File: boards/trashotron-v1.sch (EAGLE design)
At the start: 6 parts, among them IC1 MCP604P, IC2 MCP604P, J3 455-1750-1-ND

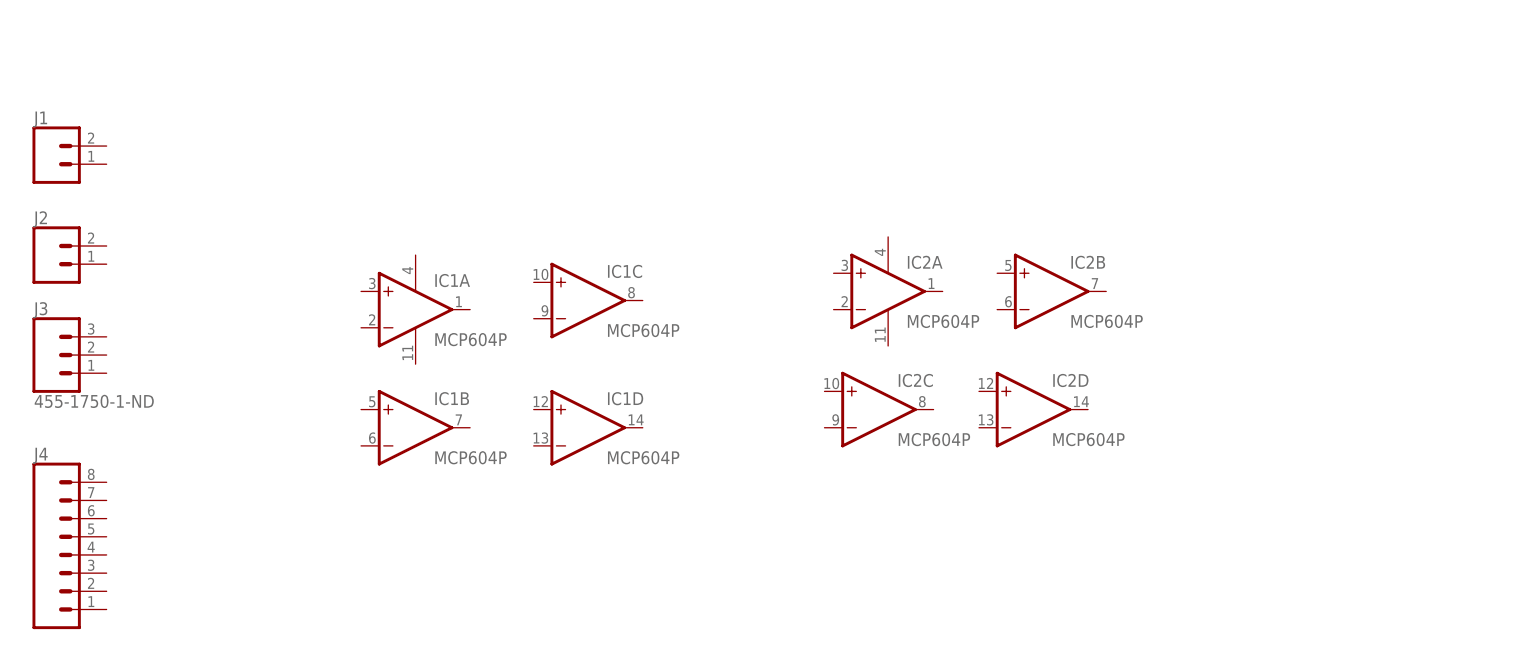
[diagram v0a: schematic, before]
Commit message: trashotron board mostly laid out in schematic
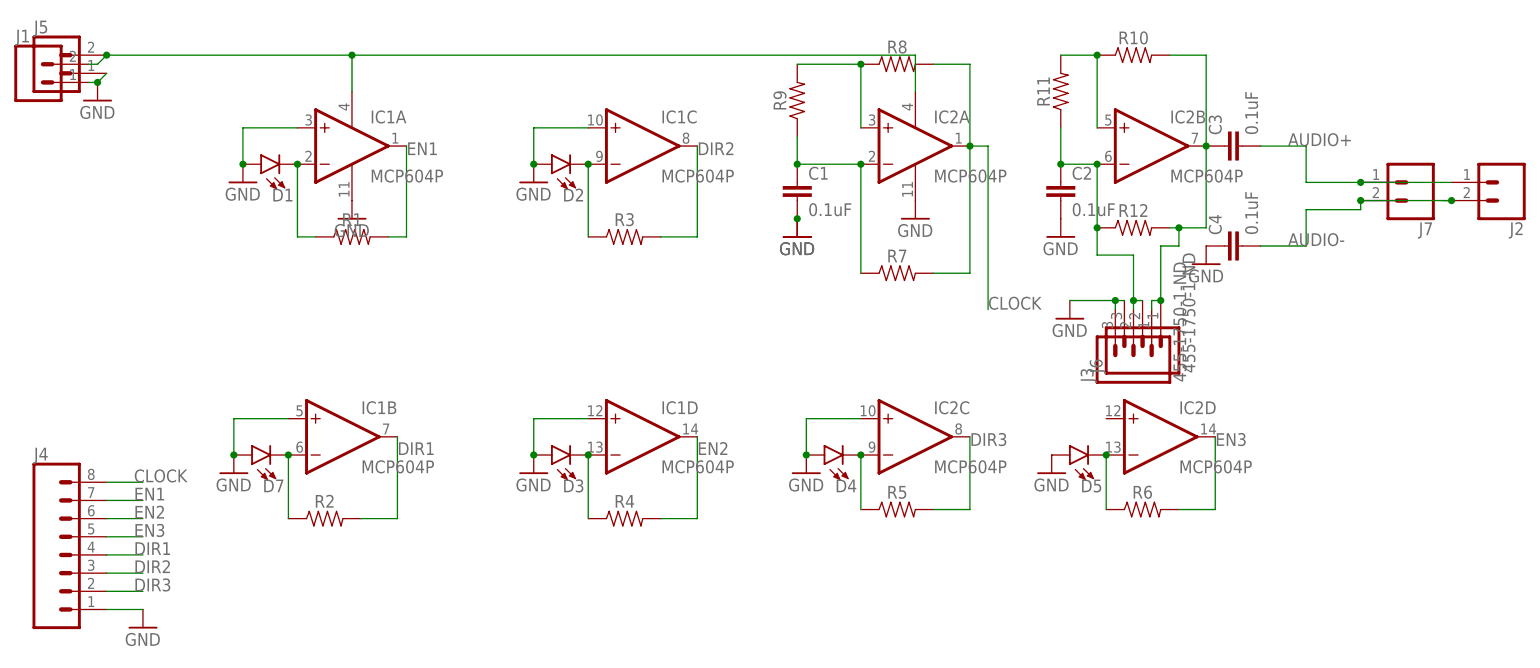
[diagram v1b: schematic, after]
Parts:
- added C1, C2, C3, C4: 0.1uF, SparkFun-Capacitors:0.1UF-KIT-EZ-50V-20%
- added D1, D2, D3, D4, D5, D7: (no value), SparkFun-LED:LED3MM
- added J5, J7: (no value), SparkFun-Connectors:CONN_02
- added J6: 455-1750-1-ND, SparkFun-Connectors:CONN_03
- added R1, R10, R11, R12, R2, R3, R4, R5, R6, R7, R8, R9: (no value), SparkFun-Resistors:RESISTORAXIAL-0.3
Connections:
- new net AUDIO+: C3.2, J2.1, J7.1
- new net AUDIO-: C4.2, J2.2, J7.2
- new net CLOCK: IC2A.OUT, J4.8, R7.2, R8.2
- new net DIR1: IC1B.OUT, J4.4, R2.2
- new net DIR2: IC1C.OUT, J4.3, R3.2
- new net DIR3: IC2C.OUT, J4.2, R5.2
- new net EN1: IC1A.OUT, J4.7, R1.2
- new net EN2: IC1D.OUT, J4.6, R4.2
- new net EN3: IC2D.OUT, J4.5, R6.2
- new net GND: C1.2, C2.2, C4.1, D1.A, D2.A, D3.A, D4.A, D5.A, D7.A, IC1A.+IN, IC1B.+IN, IC1C.+IN, IC1D.+IN, IC1P.V-, IC2C.+IN, IC2P.V-, J1.1, J3.3, J4.1, J5.1, J6.3
- new net N$1: D1.C, IC1A.-IN, R1.1
- new net N$11: D5.C, IC2D.-IN, R6.1
- new net N$13: D3.C, IC1D.-IN, R4.1
- new net N$15: C2.1, IC2B.-IN, J3.2, J6.2, R11.1, R12.1
- new net N$16: IC2A.+IN, R8.1, R9.2
- new net N$18: IC2B.+IN, R10.1, R11.2
- new net N$19: IC1P.V+, IC2P.V+, J1.2, J5.2
- new net N$24: C1.1, IC2A.-IN, R7.1, R9.1
- new net N$25: C3.1, IC2B.OUT, J3.1, J6.1, R10.2, R12.2
- new net N$5: D7.C, IC1B.-IN, R2.1
- new net N$7: D2.C, IC1C.-IN, R3.1
- new net N$9: D4.C, IC2C.-IN, R5.1
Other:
- moved on the sheet: IC1A, IC1B, IC1C, IC1D, IC2A, IC2B, IC2C, IC2D, J1, J2, J3
